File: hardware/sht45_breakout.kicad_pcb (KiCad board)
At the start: 2 copper layers, 10.2 x 12.5 mm, 6 parts, among them J1 I2C, U1 SHT45-AD1B-R2

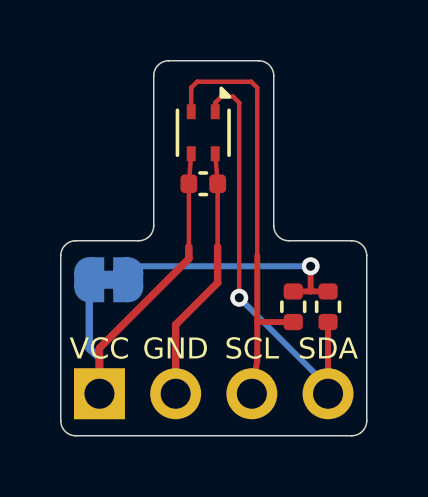
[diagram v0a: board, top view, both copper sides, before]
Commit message: Switch passives from 0402 to 0603 for hand assembly
Widen the sensor tongue to 4.4 mm so the 0603 decoupling cap still sits
right below the SHT45 with the SDA/SCL lanes beside it, and restack the
pull-ups in the base. Update LCSC numbers (C14663, C25804) and add a
hand-assembly parts list to the README. DRC and schematic/PCB net
comparison still clean.

Co-Authored-By: Claude Opus 5.5 <noreply@anthropic.com>
Claude-Session: https://claude.ai/code/session_01Cw4qgvdZTYbLFFCGBumb2e
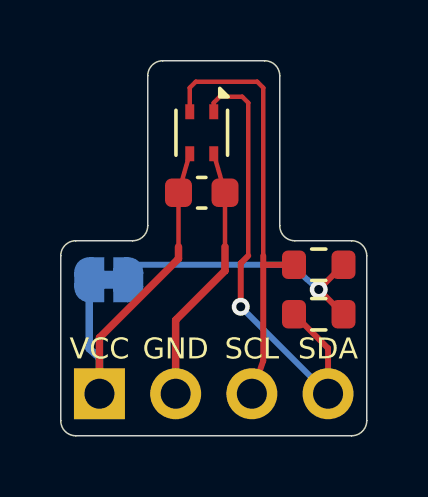
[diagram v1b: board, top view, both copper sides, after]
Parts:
- C1: footprint Capacitor_SMD:C_0402_1005Metric -> Capacitor_SMD:C_0603_1608Metric
- R1, R2: footprint Resistor_SMD:R_0402_1005Metric -> Resistor_SMD:R_0603_1608Metric
- moved R2 1.64 mm to (108.6, 106.8), turned to 180 degrees
- moved R1 0.40 mm to (108.6, 108.5), turned to 180 degrees
- moved C1 0.30 mm to (104.7, 104.4)
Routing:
- net /SDA: track 14.6 -> 15.8 mm
- net /PU: track 8.53 -> 9.49 mm
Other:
- outline, holes or cut-outs redrawn
